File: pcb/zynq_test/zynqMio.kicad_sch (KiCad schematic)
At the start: 30 parts, among them SW201 SW_SPDT, SW202 SW_SPDT, SW203 SW_SPDT, U1 XC7Z020-2CLG400I, U201 DSC1001CI2-033.3300

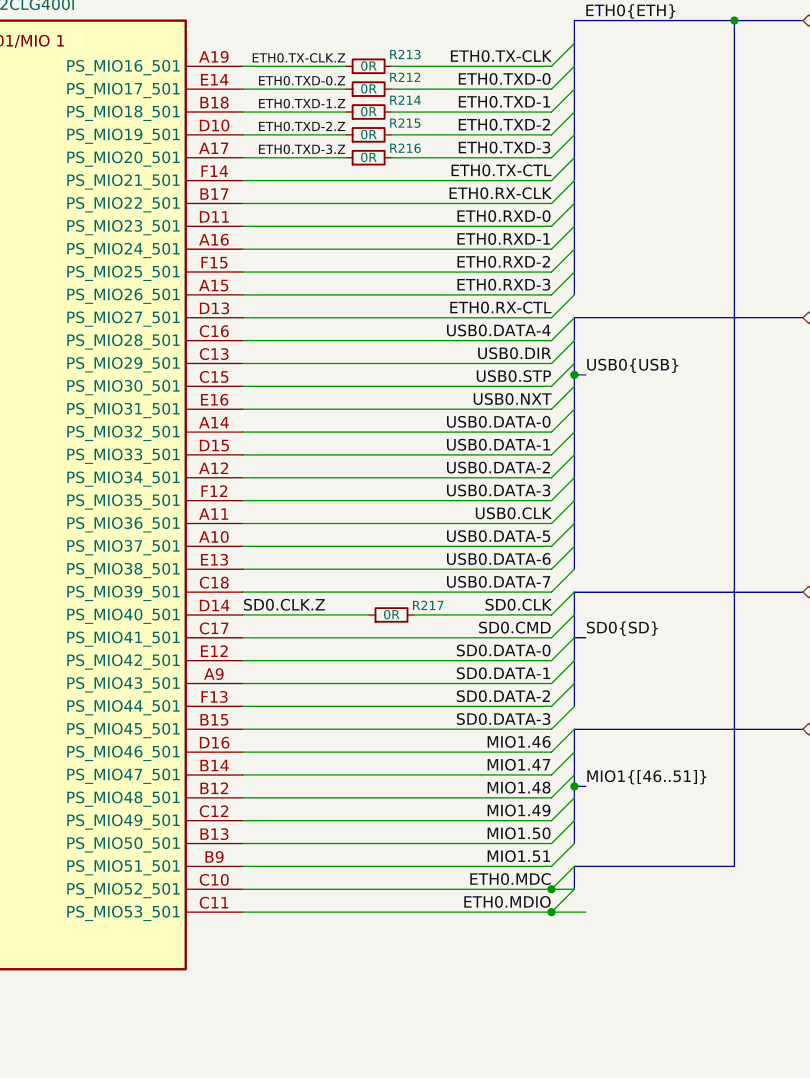
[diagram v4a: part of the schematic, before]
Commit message: Finished Ethernet, swapped FTDI chip for QFN
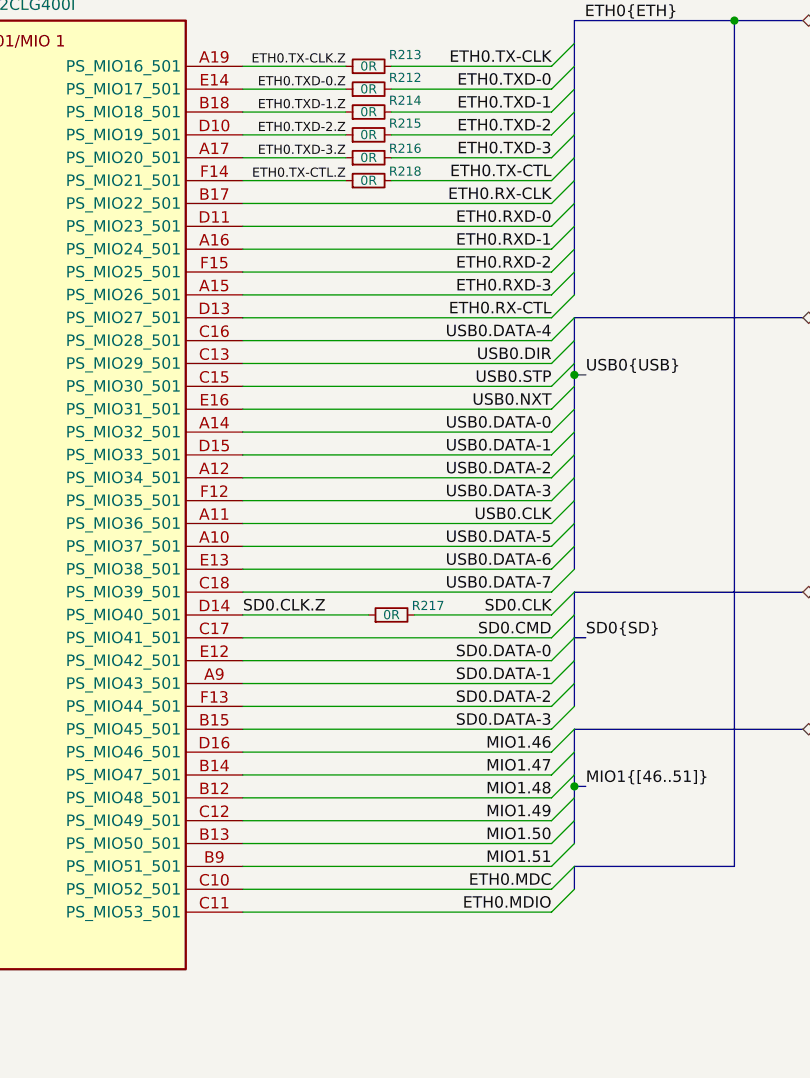
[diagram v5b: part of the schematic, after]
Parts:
- added R218: 0R, symbol Device:R_Small
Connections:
- net ETH0.TX-CTL: now also R218.2; no longer U1.F14 (PS_MIO21_501)
- new net ETH0.TX-CTL.Z: R218.1, U1.F14 (PS_MIO21_501)
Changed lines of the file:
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@@
 	)
 	(junction
-		(at 247.65 134.62)
-		(diameter 0)
-		(color 0 0 0 0)
-	)
-	(junction
 		(at 267.97 35.56)
 		(diameter 0)
@@
 	)
 	(junction
-		(at 247.65 132.08)
-		(diameter 0)
-		(color 0 0 0 0)
-	)
-	(junction
 		(at 158.75 95.25)
 		(diameter 0)
@@
 		)
 	)
-	(wire
+	(bus
 		(pts
-			(xy 213.36 53.34) (xy 247.65 53.34)
+			(xy 132.08 26.67) (xy 132.08 73.66)
 		)
 		(stroke
@@
 		)
 	)
-	(bus
+	(wire
 		(pts
-			(xy 132.08 26.67) (xy 132.08 73.66)
+			(xy 137.16 41.91) (xy 137.16 40.64)
 		)
 		(stroke
@@
 		)
 	)
-	(wire
+	(bus
 		(pts
-			(xy 137.16 41.91) (xy 137.16 40.64)
+			(xy 250.19 132.08) (xy 250.19 129.54)
 		)
 		(stroke
@@
 		)
 	)
-	(bus
+	(wire
 		(pts
-			(xy 250.19 132.08) (xy 250.19 129.54)
+			(xy 229.87 53.34) (xy 247.65 53.34)
 		)
 		(stroke
@@
 	(wire
 		(pts
+			(xy 213.36 53.34) (xy 224.79 53.34)
+		)
+		(stroke
+			(width 0)
+			(type default)
+		)
+	)
+	(wire
+		(pts
 			(xy 87.63 48.26) (xy 124.46 48.26)
 		)
@@
 	(wire
 		(pts
-			(xy 247.65 134.62) (xy 251.46 134.62)
-		)
-		(stroke
-			(width 0)
-			(type default)
-		)
-	)
-	(wire
-		(pts
 			(xy 29.21 50.8) (xy 29.21 53.34)
 		)
@@
 		)
 	)
-	(wire
-		(pts
-			(xy 247.65 132.08) (xy 250.19 132.08)
-		)
-		(stroke
-			(width 0)
-			(type default)
-		)
-	)
 	(bus
 		(pts
@@
 		)
 	)
+	(label "ETH0.TX-CTL.Z"
+		(at 224.79 53.34 180)
+		(effects
+			(font
+				(size 1.016 1.016)
+			)
+			(justify right bottom)
+		)
+	)
 	(label "ETH0{ETH}"
 		(at 261.62 35.56 180)
@@
 					(unit 1)
 				)
+			)
+		)
+	)
+	(symbol
+		(lib_id "Device:R_Small")
+		(at 227.33 53.34 90)
+		(unit 1)
+		(exclude_from_sim no)
+		(in_bom yes)
+		(on_board yes)
+		(dnp no)
+		(property "Reference" "R218"
+			(at 231.394 52.324 90)
+			(effects
+				(font
+					(size 1.016 1.016)
+				)
+			)
+		)
+		(property "Value" "0R"
+			(at 227.33 53.34 90)
+			(effects
+				(font
+					(size 1.016 1.016)
+				)
+			)
+		)
+		(property "Footprint" ""
+			(at 227.33 53.34 0)
+			(effects
+				(font
+					(size 1.27 1.27)
+				)
+				(hide yes)
+			)
+		)
+		(property "Datasheet" "~"
+			(at 227.33 53.34 0)
+			(effects
+				(font
+					(size 1.27 1.27)
+				)
+				(hide yes)
+			)
+		)
+		(property "Description" "Resistor, small symbol"
+			(at 227.33 53.34 0)
+			(effects
+				(font
+					(size 1.27 1.27)
+				)
+				(hide yes)
+			)
+		)
+		(pin "1"
+		)
+		(pin "2"
+		)
+		(instances
+			(project "zynq_test"
+				(path "/0637578d-4ce5-4d31-b973-2de977269ea5/db3711b0-f4a6-4694-bd1d-6c88710ed953"
+					(reference "R218")
+					(unit 1)
+				)

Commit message: Finished HDMI
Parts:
- U1: footprint Zynq:CLG400_ZYNQ-7000_AMD -> Package_BGA:Xilinx_CLG400
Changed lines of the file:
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@@
 			)
 		)
-		(property "Footprint" "Zynq:CLG400_ZYNQ-7000_AMD"
+		(property "Footprint" "Package_BGA:Xilinx_CLG400"
 			(at 34.29 -16.51 0)
 			(effects
@@
 			)
 		)
-		(property "Footprint" "Zynq:CLG400_ZYNQ-7000_AMD"
+		(property "Footprint" "Package_BGA:Xilinx_CLG400"
 			(at 157.48 13.97 0)
 			(effects

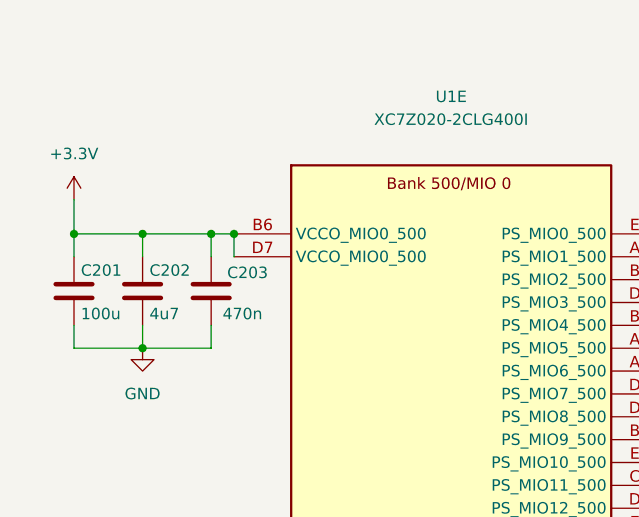
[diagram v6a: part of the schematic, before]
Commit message: Started on DDR3
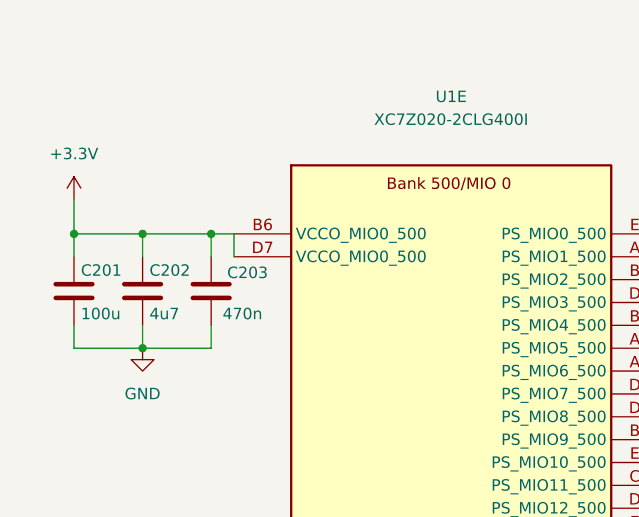
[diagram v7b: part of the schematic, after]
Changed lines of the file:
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@@
-	)
-	(junction
-		(at 39.37 40.64)
-		(diameter 0)
-		(color 0 0 0 0)
 	)
 	(junction

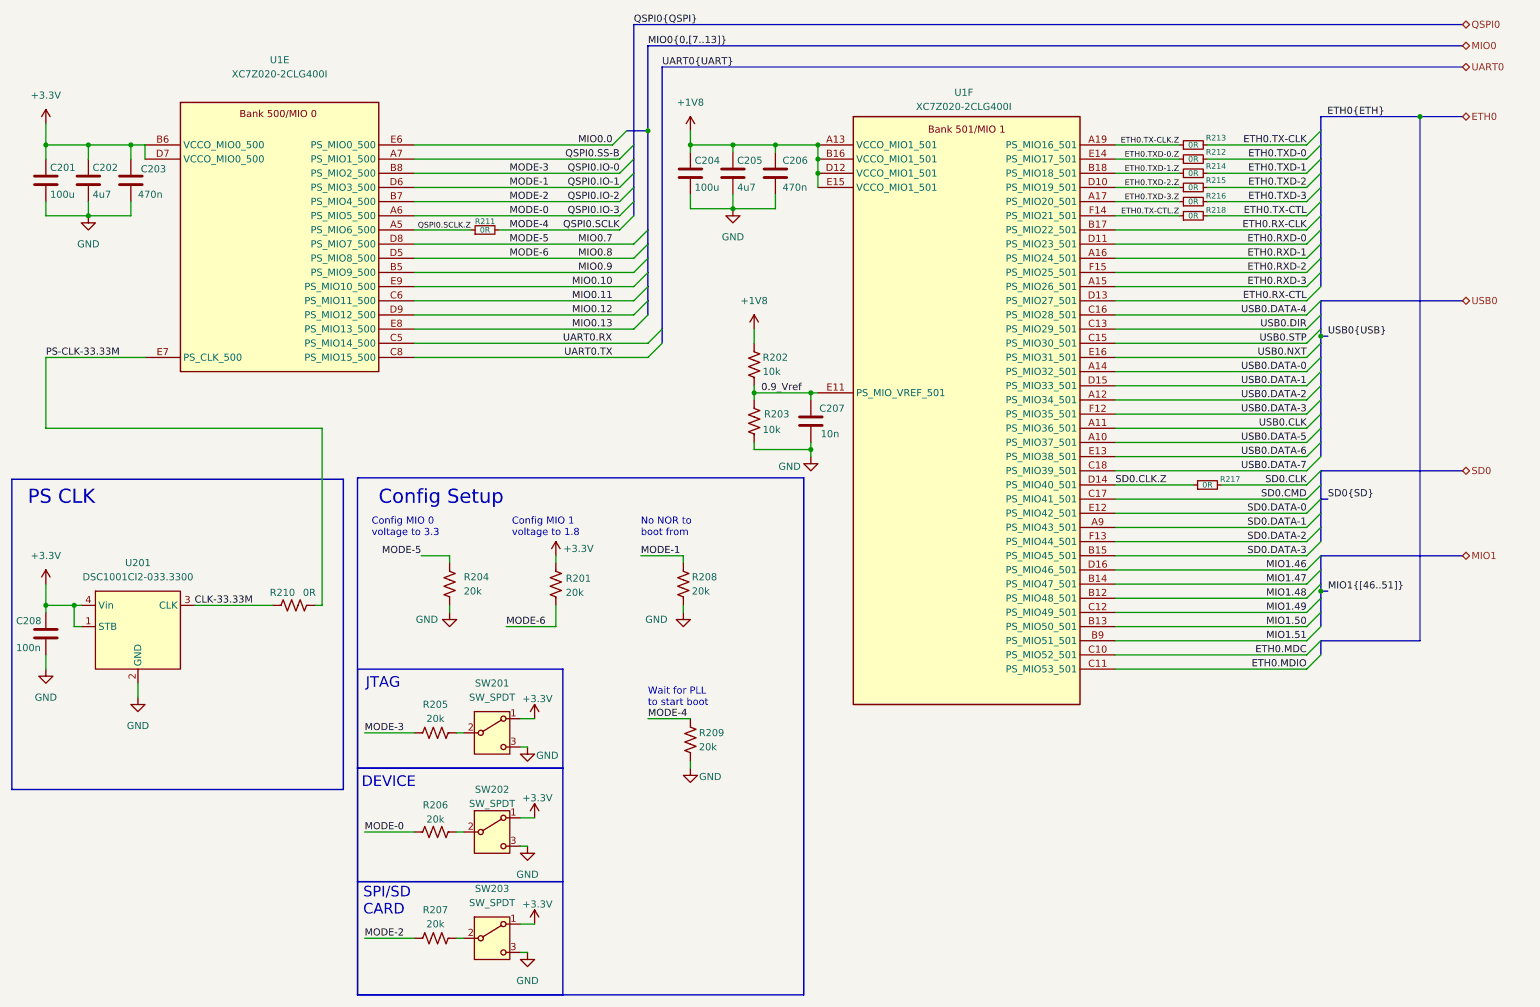
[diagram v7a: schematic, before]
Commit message: Connected DDR3, cleaned up some thing
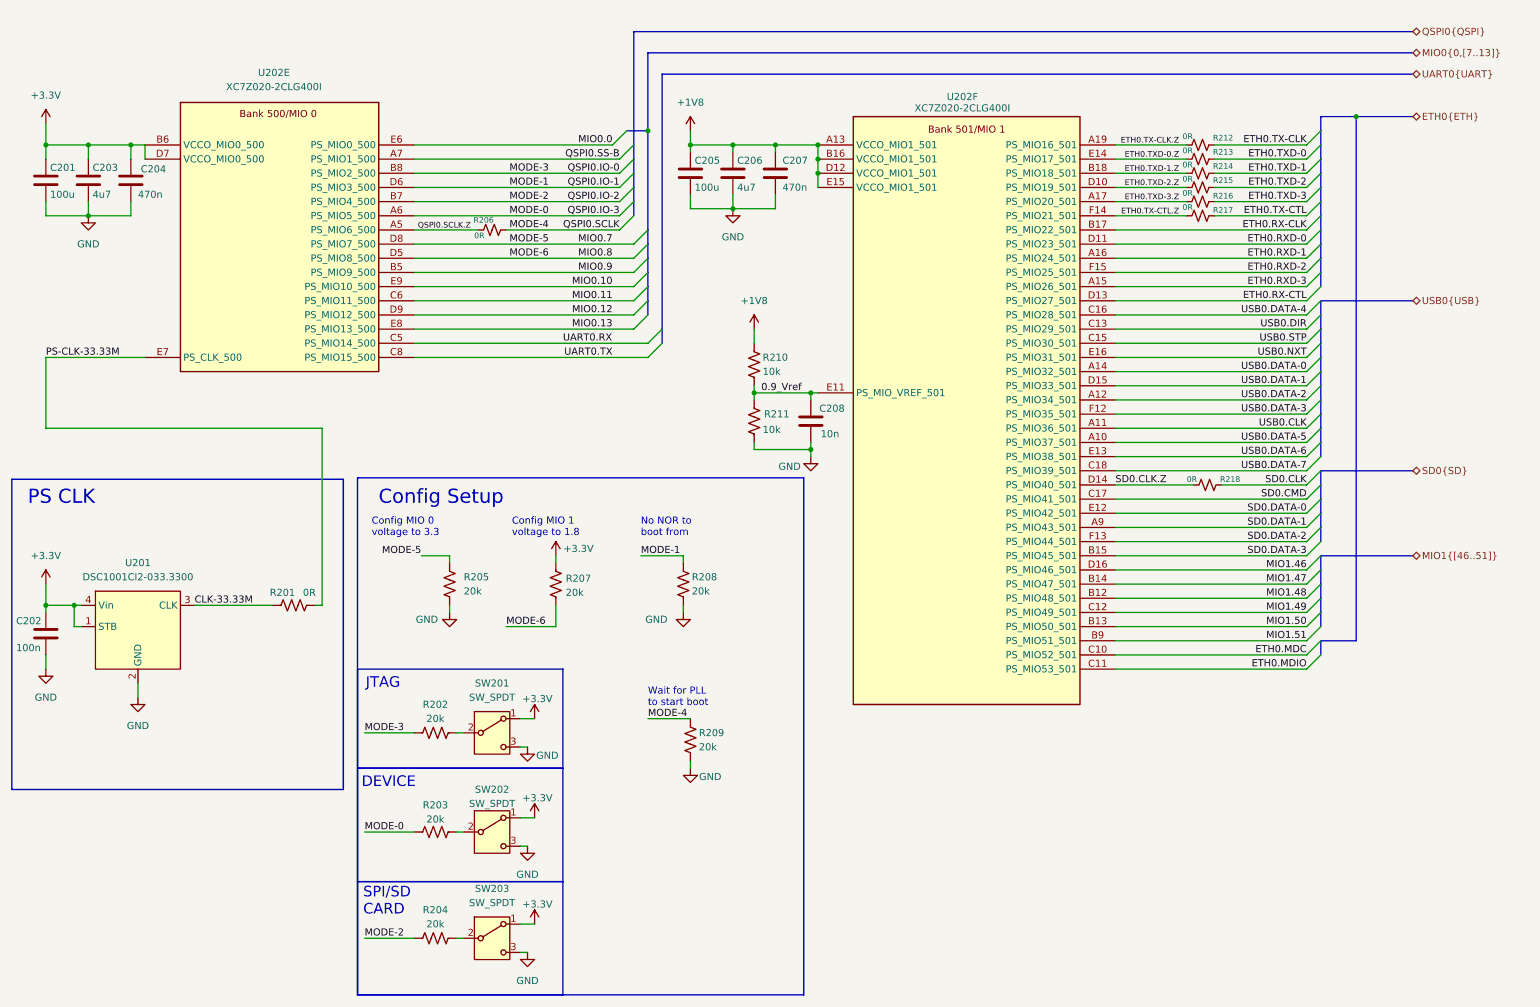
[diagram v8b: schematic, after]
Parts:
- R206: renamed from R211; symbol Device:R_Small -> Device:R_Small_US
- R212: renamed from R213; symbol Device:R_Small -> Device:R_Small_US
- R213: renamed from R212; symbol Device:R_Small -> Device:R_Small_US
- R214, R215, R216: symbol Device:R_Small -> Device:R_Small_US
- R217: renamed from R218; symbol Device:R_Small -> Device:R_Small_US
- R218: renamed from R217; symbol Device:R_Small -> Device:R_Small_US
- renumbered C208 to C202, C202 to C203, C203 to C204, C204 to C205, C205 to C206, C206 to C207, C207 to C208, R210 to R201, R205 to R202, R206 to R203, R207 to R204, R204 to R205, R201 to R207, R202 to R210, R203 to R211, U1 to U202
